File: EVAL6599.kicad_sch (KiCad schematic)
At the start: 0 parts

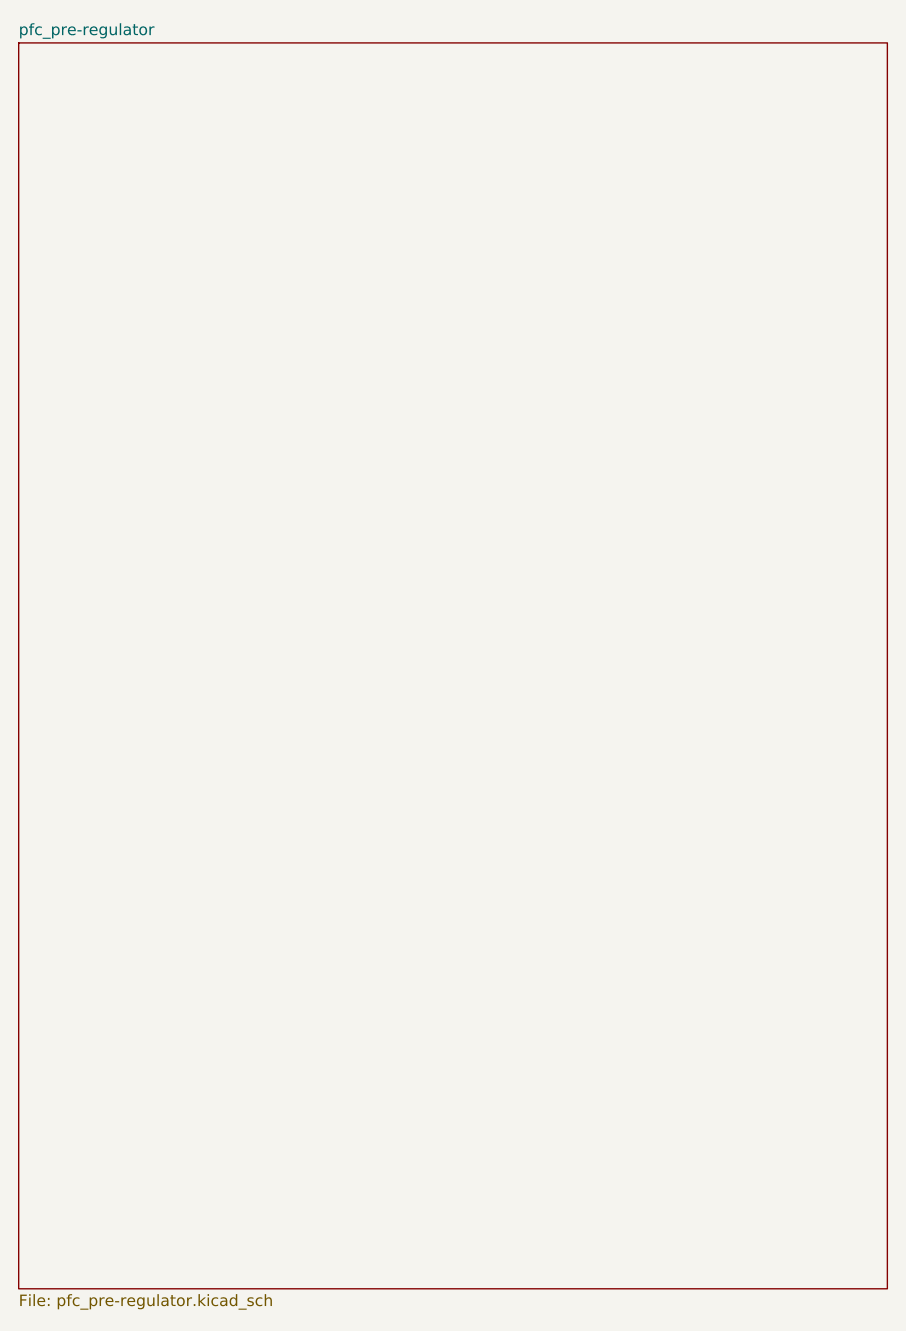
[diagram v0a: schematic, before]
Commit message: Added the other sub-schematics of the design
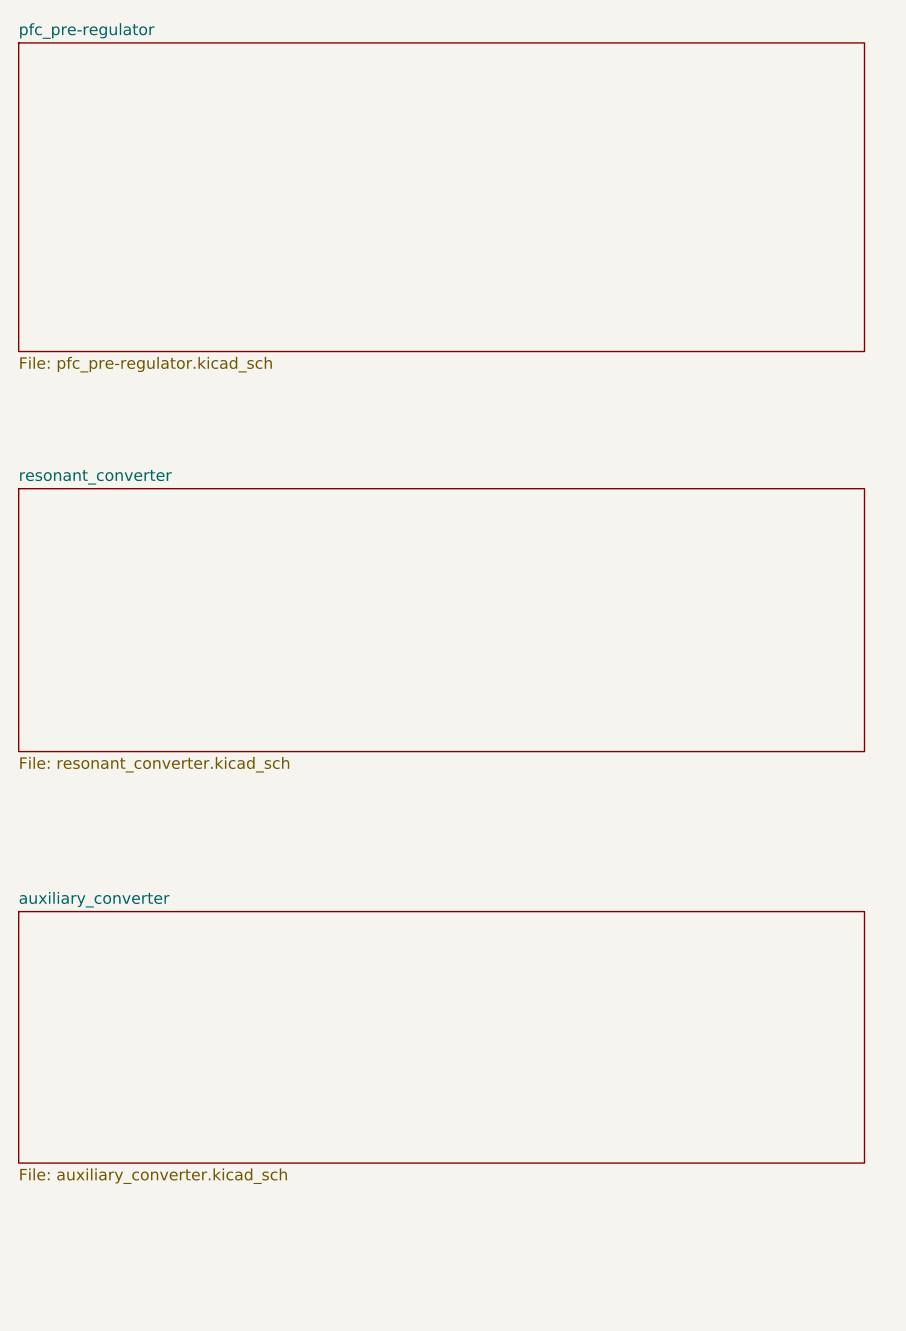
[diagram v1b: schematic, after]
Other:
- added sheet auxiliary_converter (auxiliary_converter.kicad_sch)
- added sheet resonant_converter (resonant_converter.kicad_sch)
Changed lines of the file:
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@@
 	(paper "A4")
 	(sheet
+		(at 15.24 114.3)
+		(size 93.98 27.94)
+		(fields_autoplaced yes)
+		(stroke
+			(width 0.1524)
+			(type solid)
+		)
+		(fill
+			(color 0 0 0 0.0000)
+		)
+		(property "Sheetname" "auxiliary_converter"
+			(at 15.24 113.5884 0)
+			(effects
+				(font
+					(size 1.27 1.27)
+				)
+				(justify left bottom)
+			)
+		)
+		(property "Sheetfile" "auxiliary_converter.kicad_sch"
+			(at 15.24 142.8246 0)
+			(effects
+				(font
+					(size 1.27 1.27)
+				)
+				(justify left top)
+			)
+		)
+		(instances
+			(project "EVAL6599"
+				(path "/ab3b6b9f-35a8-4587-9dd4-e6d1eecaa4cd"
+					(page "4")
+				)
+			)
+		)
+	)
+	(sheet
 		(at 15.24 17.78)
-		(size 96.52 138.43)
+		(size 93.98 34.29)
 		(fields_autoplaced yes)
 		(stroke
@@
 		)
 		(property "Sheetfile" "pfc_pre-regulator.kicad_sch"
-			(at 15.24 156.7946 0)
+			(at 15.24 52.6546 0)
 			(effects
 				(font
@@
 				)
 			)
+		)
+	)
+	(sheet
+		(at 15.24 67.31)
+		(size 93.98 29.21)
+		(fields_autoplaced yes)
+		(stroke
+			(width 0.1524)
+			(type solid)
+		)
+		(fill
+			(color 0 0 0 0.0000)
+		)
+		(property "Sheetname" "resonant_converter"
+			(at 15.24 66.5984 0)
+			(effects
+				(font
+					(size 1.27 1.27)
+				)
+				(justify left bottom)
+			)
+		)
+		(property "Sheetfile" "resonant_converter.kicad_sch"
+			(at 15.24 97.1046 0)
+			(effects
+				(font
+					(size 1.27 1.27)
+				)
+				(justify left top)
+			)
+		)
+		(instances
+			(project "EVAL6599"
+				(path "/ab3b6b9f-35a8-4587-9dd4-e6d1eecaa4cd"
+					(page "3")
+				)
+			)
